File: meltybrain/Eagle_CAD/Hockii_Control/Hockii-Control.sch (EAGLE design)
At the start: 64 parts, among them J1 SM03B-SRSS-TB(LF)(SN), J2 SM04B-SRSS-TB(LF)(SN), J4 SM04B-SRSS-TB(LF)(SN), J7 SM02B-SRSS-TB(LF)(SN), J8 SM02B-SRSS-TB(LF)(SN), U13 TMP235A4DCKR, U14 ADXL375, U15 NL27WZ32USG, U16 ADXL375, U17 ADXL375, U18 NL27WZ32USG, U19 ADXL375, U2 TEENSY_4.1, U3 AP2210K-5.0TRG1, U5 TXS0104ED, U6 LDL212PU50R, U7 LIS3MDLTR, U8 BA50DD0WHFP-TR, X1 22-23-2021

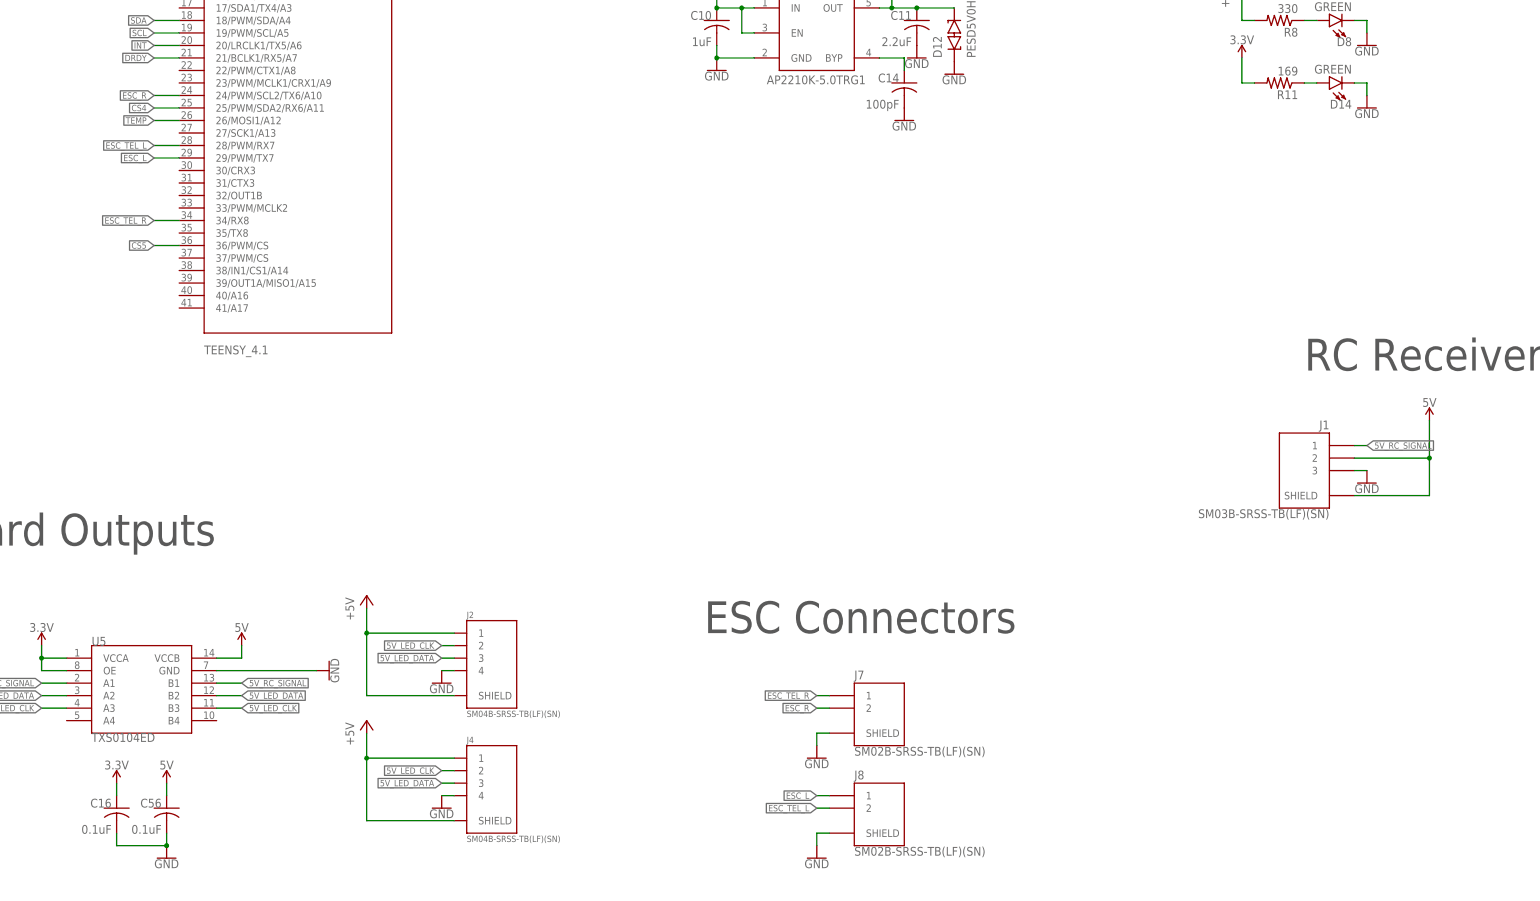
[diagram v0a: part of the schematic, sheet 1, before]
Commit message: add VESC JST
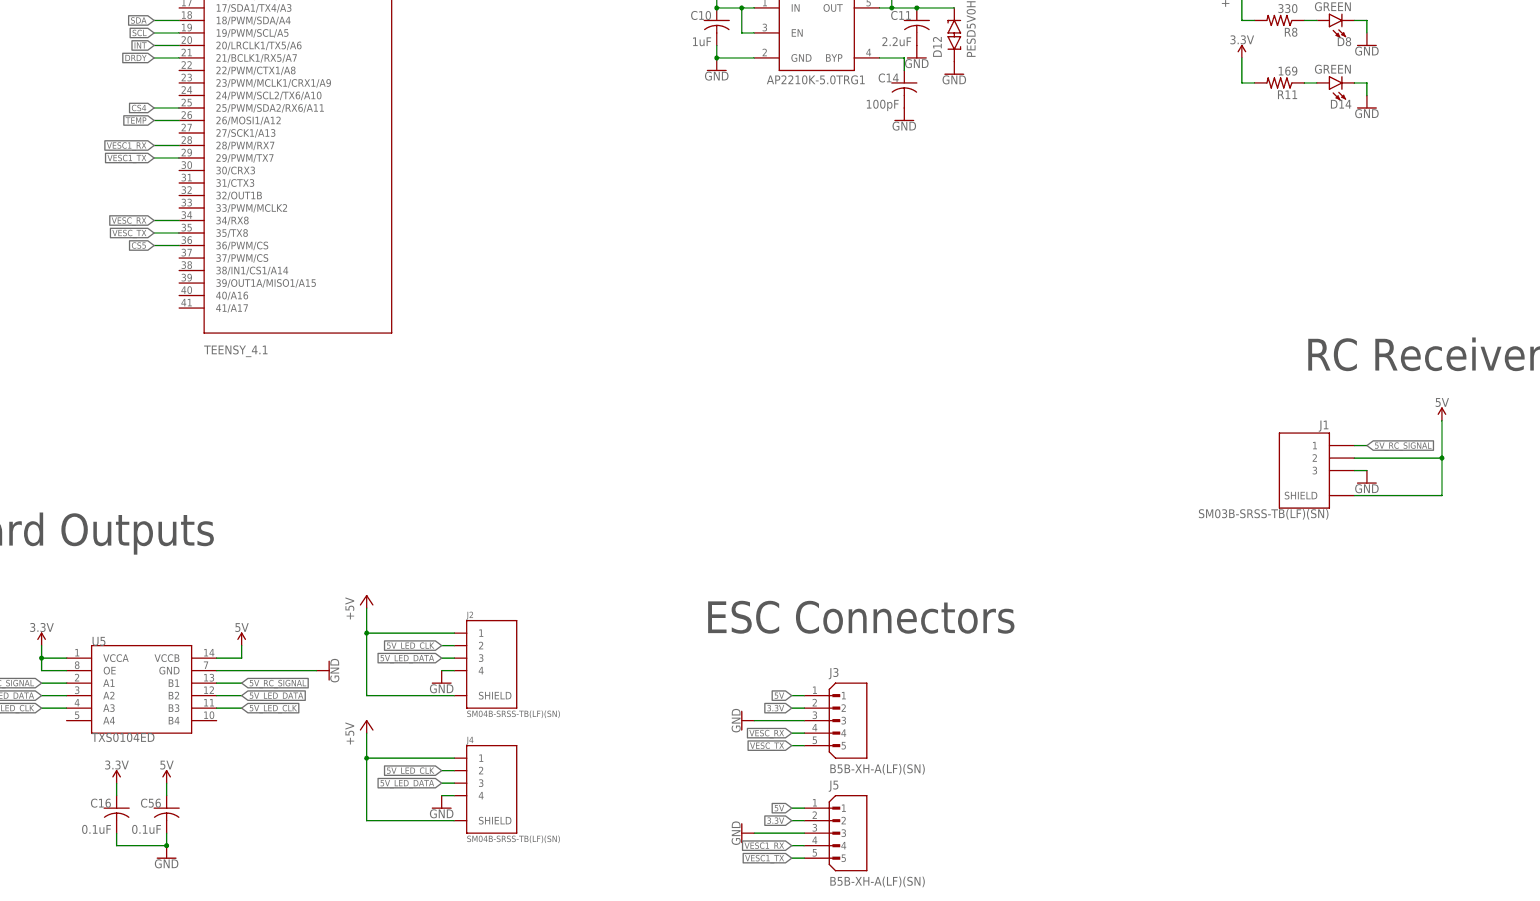
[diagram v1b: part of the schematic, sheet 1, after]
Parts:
- removed J7, J8: SM02B-SRSS-TB(LF)(SN), Hocki_Library:SM02B-SRSS-TB(LF)(SN)
- added J3, J5: B5B-XH-A(LF)(SN), Hocki_Library:B5B-XH-A(LF)(SN)
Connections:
- removed net ESC_L: J8.1, U2.29/PWM/TX7
- removed net ESC_R: J7.2, U2.24/PWM/SCL2/TX6/A10
- removed net ESC_TEL_L: J8.2, U2.28/PWM/RX7
- removed net ESC_TEL_R: J7.1, U2.34/RX8
- new net VESC1_RX: J5.4, U2.28/PWM/RX7
- new net VESC1_TX: J5.5, U2.29/PWM/TX7
- new net VESC_RX: J3.4, U2.34/RX8
- new net VESC_TX: J3.5, U2.35/TX8
- net 3.3V: now also J3.2, J5.2
- net 5V: now also J3.1, J5.1
- net GND: now also J3.3, J5.3; no longer J7.SHIELD, J8.SHIELD
